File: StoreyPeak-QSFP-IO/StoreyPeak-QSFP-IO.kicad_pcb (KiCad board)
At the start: 2 copper layers, 30.1 x 69.8 mm, 33 parts, among them U1 QSFP_PCB-QSFP, U3 CH340G, X1 X322512MSB4SI

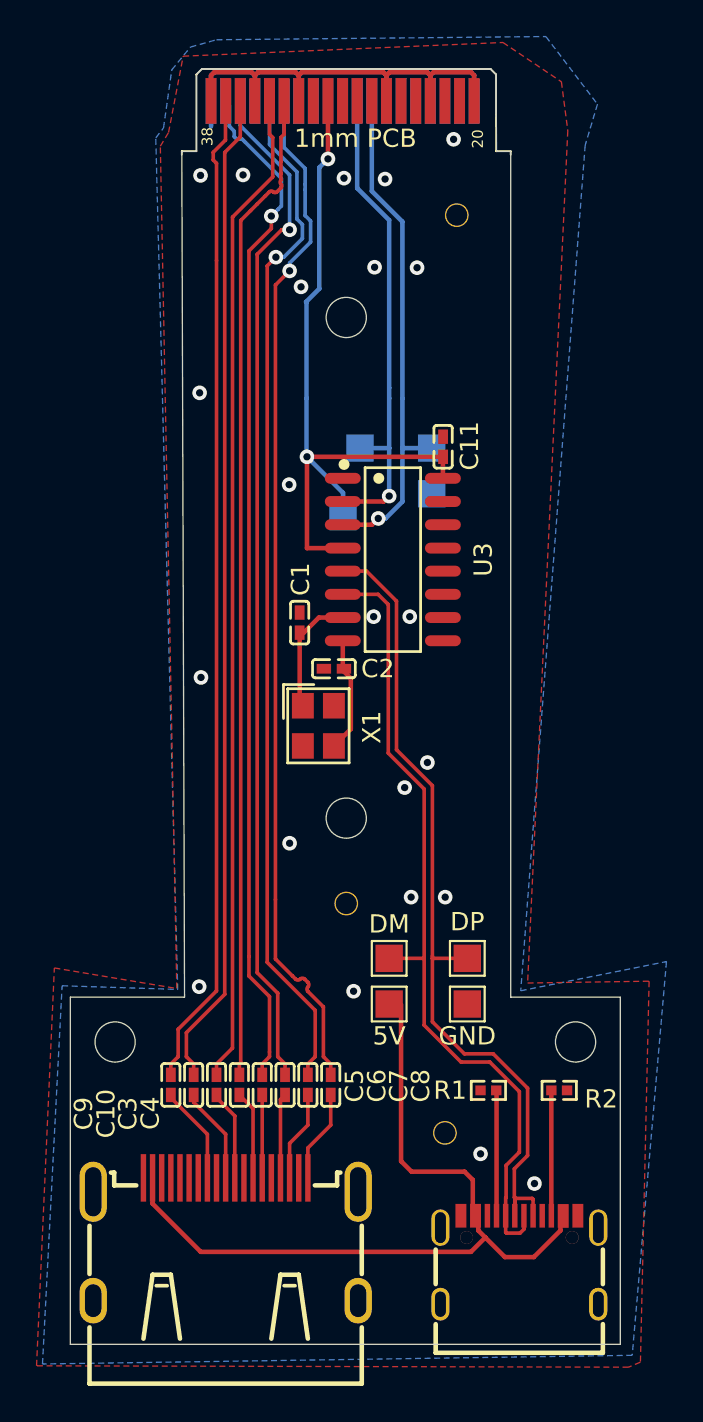
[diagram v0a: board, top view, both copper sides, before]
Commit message: Get 3.3V from LDO off USB port
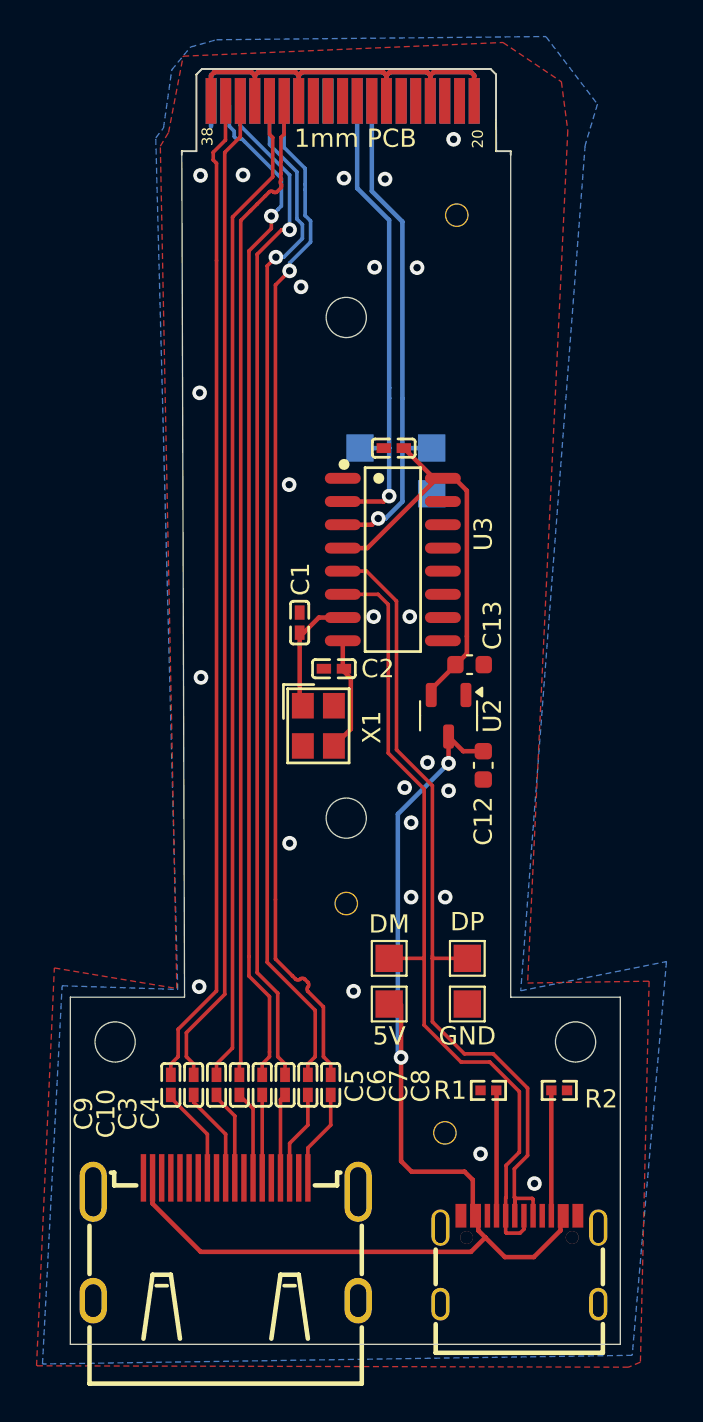
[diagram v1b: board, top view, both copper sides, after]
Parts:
- removed TP8: 3v3, TestPoint:TestPoint_Pad_1.5x1.5mm
- added C12: CL10A105KO8NNNC, Capacitor_SMD:C_0603_1608Metric, F.Cu at (169.5, 101.3)
- added C13: CL10A105KO8NNNC, Capacitor_SMD:C_0603_1608Metric, F.Cu at (168.8, 95.8)
- added U2: XC6206P62xMR, Package_TO_SOT_SMD:SOT-23-3, F.Cu at (167.6, 98.6)
- moved C11 2.70 mm to (164.6, 84.0), turned to 0 degrees
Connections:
- net /USB_D+ renamed USB_D+
- net /USB_D- renamed USB_D-
- HDMI1 pad 11: GND -> Net-(HDMI1-CK_SHIELD)
- HDMI1 pad 17: GND -> Net-(HDMI1-CK_SHIELD)
- HDMI1 pad 2: GND -> Net-(HDMI1-CK_SHIELD)
- HDMI1 pad 20: GND -> Net-(HDMI1-CK_SHIELD)
- HDMI1 pad 21: GND -> Net-(HDMI1-CK_SHIELD)
- HDMI1 pad 22: GND -> Net-(HDMI1-CK_SHIELD)
- HDMI1 pad 23: GND -> Net-(HDMI1-CK_SHIELD)
- HDMI1 pad 5: GND -> Net-(HDMI1-CK_SHIELD)
- HDMI1 pad 8: GND -> Net-(HDMI1-CK_SHIELD)
- U1 pad 30: +3V3 -> unconnected-(U1-Vcc1-Pad30)
- USB1 pad A1: GND -> unconnected-(USB1-GND-PadA1)
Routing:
- net +5V: track 43.2 -> 64.6 mm, vias 0 -> 2
- net +3V3: track 40.0 -> 23.2 mm, vias 2 -> 0
- net GND: vias 22 -> 24

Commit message: Connect HDMI ground pins
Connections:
- HDMI1 pad 11: Net-(HDMI1-CK_SHIELD) -> GND
- HDMI1 pad 17: Net-(HDMI1-CK_SHIELD) -> GND
- HDMI1 pad 2: Net-(HDMI1-CK_SHIELD) -> GND
- HDMI1 pad 20: Net-(HDMI1-CK_SHIELD) -> GND
- HDMI1 pad 21: Net-(HDMI1-CK_SHIELD) -> GND
- HDMI1 pad 22: Net-(HDMI1-CK_SHIELD) -> GND
- HDMI1 pad 23: Net-(HDMI1-CK_SHIELD) -> GND
- HDMI1 pad 5: Net-(HDMI1-CK_SHIELD) -> GND
- HDMI1 pad 8: Net-(HDMI1-CK_SHIELD) -> GND

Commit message: Remove 3V3 text on back
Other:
- board text removed: "3V3"
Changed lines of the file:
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@@
-		)
-	)
-	(gr_text "3V3"
-		(at 161.85 89.675 -0)
-		(layer "B.SilkS")
-		(effects
-			(font
-				(size 1 1)
-				(thickness 0.15)
-			)
-			(justify mirror)
 		)
 	)

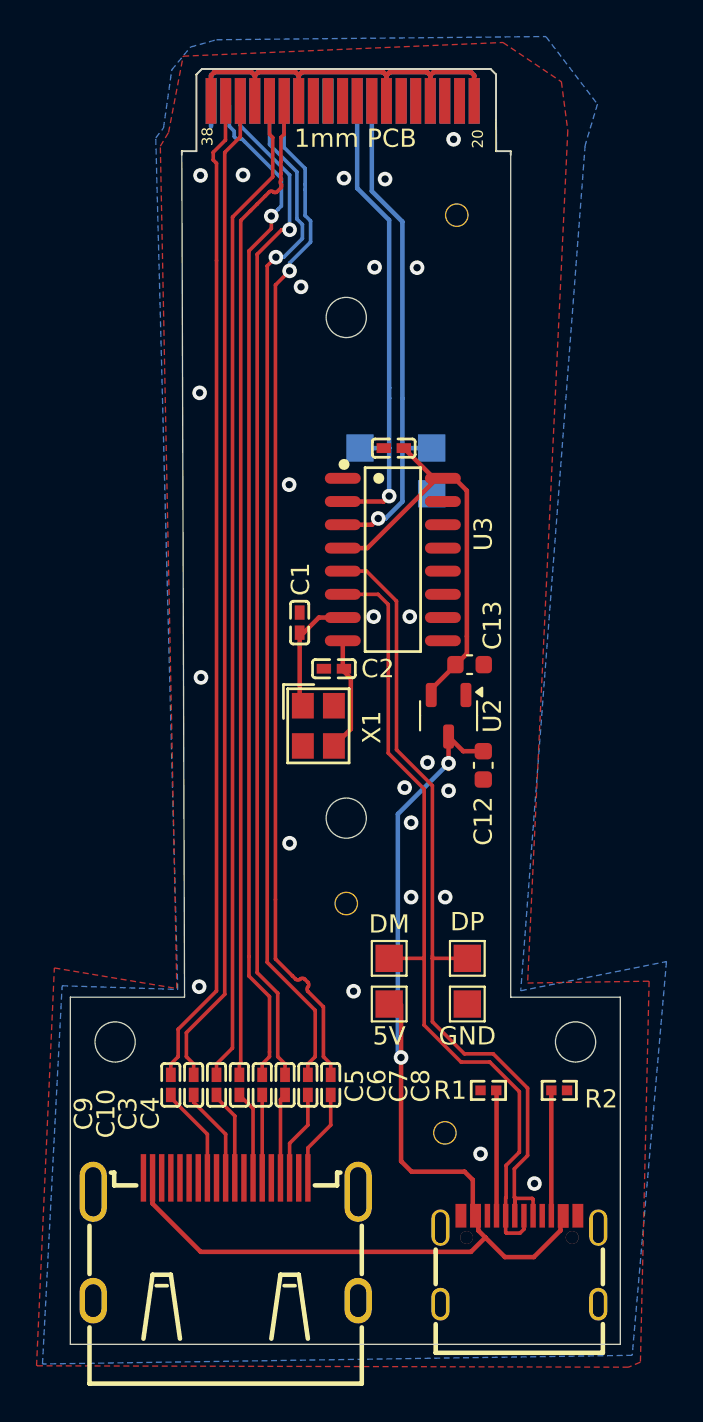
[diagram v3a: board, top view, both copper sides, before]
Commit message: Fix wrong footprint for QSFP edge connector
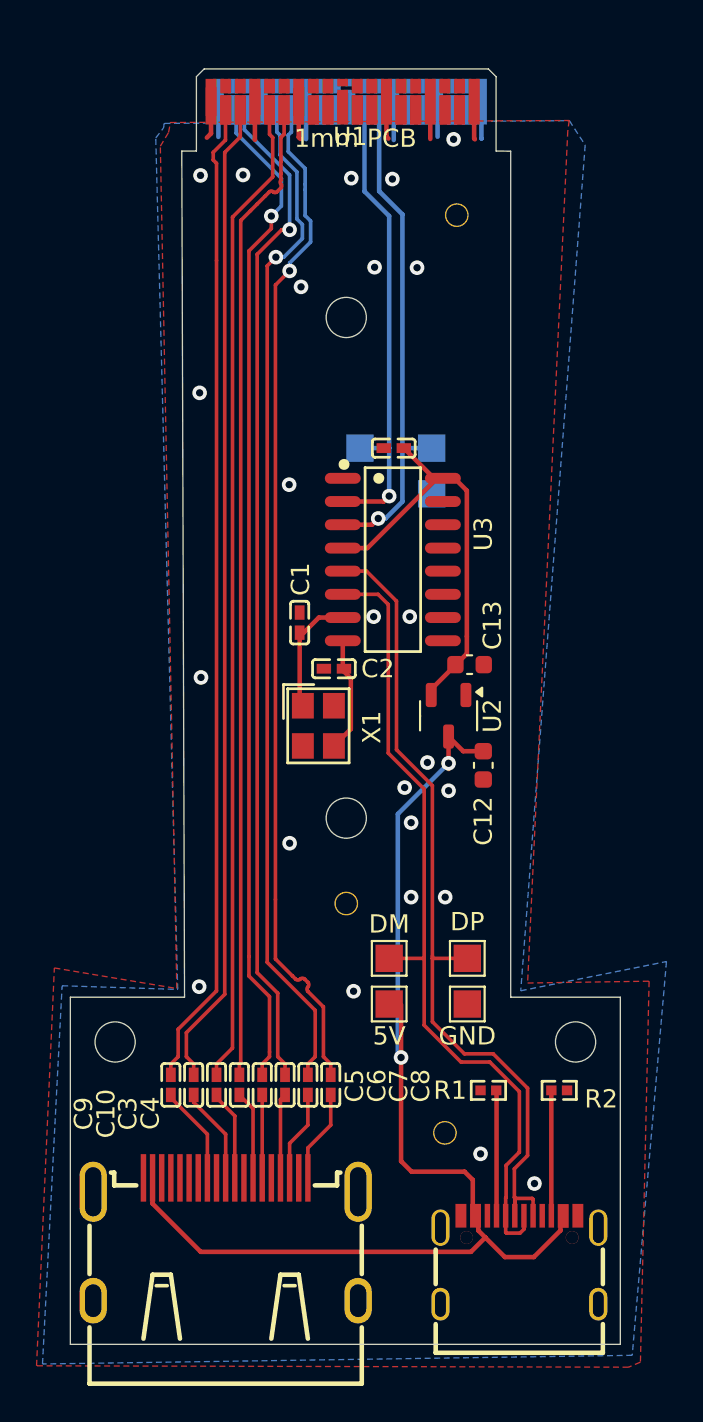
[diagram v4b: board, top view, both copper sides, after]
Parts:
- U1: footprint CarlosEDP_Lib:QSFP_PCB -> natanbc:QSFP-Edge
- moved U1 8.47 mm to (162.0, 63.2)
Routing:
- net GND: track 48.6 -> 22.7 mm
- net QSFP_D1-: track 56.1 -> 55.3 mm
- net QSFP_D2-: track 56.3 -> 55.7 mm
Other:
- outline, holes or cut-outs redrawn

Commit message: Readd 3V3 test point
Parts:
- added 3V3: 3V3, TestPoint:TestPoint_Pad_1.5x1.5mm, B.Cu at (162.8, 86.5)
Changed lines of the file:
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@@
 		)
 		(property "Value" "FPGA_TX"
-			(at 0 2.05 0)
+			(at -2.925 1.69 90)
 			(layer "B.SilkS")
 			(effects
@@
 			(layers "B.Cu" "B.Mask")
 			(net 27 "FPGA_TX")
+			(pinfunction "1")
+			(pintype "passive")
+		)
+		(embedded_fonts no)
+	)
+	(footprint "TestPoint:TestPoint_Pad_1.5x1.5mm"
+		(layer "B.Cu")
+		(at 162.75 86.45)
+		(descr "SMD rectangular pad as test Point, square 1.5mm side length")
+		(tags "test point SMD pad rectangle square")
+		(property "Reference" "3V3"
+			(at -2.76 0.5 180)
+			(layer "B.SilkS")
+			(effects
+				(font
+					(size 1 1)
+					(thickness 0.15)
+				)
+				(justify mirror)
+			)
+		)
+		(property "Value" "3V3"
+			(at 0 -1.75 180)
+			(layer "B.Fab")
+			(effects
+				(font
+					(size 1 1)
+					(thickness 0.15)
+				)
+				(justify mirror)
+			)
+		)
+		(property "Datasheet" "~"
+			(at 0 0 180)
+			(unlocked yes)
+			(layer "B.Fab")
+			(hide yes)
+			(effects
+				(font
+					(size 1.27 1.27)
+					(thickness 0.15)
+				)
+				(justify mirror)
+			)
+		)
+		(property "Description" "test point"
+			(at 0 0 180)
+			(unlocked yes)
+			(layer "B.Fab")
+			(hide yes)
+			(effects
+				(font
+					(size 1.27 1.27)
+					(thickness 0.15)
+				)
+				(justify mirror)
+			)
+		)
+		(property ki_fp_filters "Pin* Test*")
+		(sheetname "/")
+		(sheetfile "StoreyPeak-QSFP-IO.kicad_sch")
+		(attr exclude_from_pos_files)
+		(fp_line
+			(start -0.95 -0.95)
+			(end -0.95 0.95)
+			(stroke
+				(width 0.12)
+				(type solid)
+			)
+			(layer "B.SilkS")
+		)
+		(fp_line
+			(start -0.95 0.95)
+			(end 0.95 0.95)
+			(stroke
+				(width 0.12)
+				(type solid)
+			)
+			(layer "B.SilkS")
+		)
+		(fp_line
+			(start 0.95 -0.95)
+			(end -0.95 -0.95)
+			(stroke
+				(width 0.12)
+				(type solid)
+			)
+			(layer "B.SilkS")
+		)
+		(fp_line
+			(start 0.95 0.95)
+			(end 0.95 -0.95)
+			(stroke
+				(width 0.12)
+				(type solid)
+			)
+			(layer "B.SilkS")
+		)
+		(fp_line
+			(start -1.25 1.25)
+			(end -1.25 -1.25)
+			(stroke
+				(width 0.05)
+				(type solid)
+			)
+			(layer "B.CrtYd")
+		)
+		(fp_line
+			(start -1.25 1.25)
+			(end 1.25 1.25)
+			(stroke
+				(width 0.05)
+				(type solid)
+			)
+			(layer "B.CrtYd")
+		)
+		(fp_line
+			(start 1.25 -1.25)
+			(end -1.25 -1.25)
+			(stroke
+				(width 0.05)
+				(type solid)
+			)
+			(layer "B.CrtYd")
+		)
+		(fp_line
+			(start 1.25 -1.25)
+			(end 1.25 1.25)
+			(stroke
+				(width 0.05)
+				(type solid)
+			)
+			(layer "B.CrtYd")
+		)
+		(fp_text user "${REFERENCE}"
+			(at 0 1.65 180)
+			(layer "B.Fab")
+			(effects
+				(font
+					(size 1 1)
+					(thickness 0.15)
+				)
+				(justify mirror)
+			)
+		)
+		(pad "1" smd rect
+			(at 0 0)
+			(size 1.5 1.5)
+			(layers "B.Cu" "B.Mask")
+			(net 41 "+3V3")
 			(pinfunction "1")
 			(pintype "passive")
@@
 		)
 		(property "Value" "FPGA_RX"
-			(at 0.5 -1.75 0)
+			(at 2.72 1.68 90)
 			(layer "B.SilkS")
 			(effects
@@
 	)
 	(gr_text "GND"
-		(at 166.675 88.2 -0)
+		(at 169.43 87.11 -0)
 		(layer "B.SilkS")
 		(effects
